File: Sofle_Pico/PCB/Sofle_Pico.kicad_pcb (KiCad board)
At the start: 2 copper layers, 145.4 x 116.3 mm, 124 parts, among them J1 Conn_01x05, J2 4PIN, J3 Conn_01x04, J4 Conn_01x04, J5 Conn_02x05_Odd_Even, J7 Conn_01x04, Q1 Si2301CDS, SW1 SW_PUSH, SW10 SW_PUSH, SW11 SW_PUSH, SW12 SW_PUSH, SW13 SW_PUSH, SW14 SW_PUSH, SW15 SW_PUSH, SW16 SW_PUSH, SW17 SW_PUSH, SW18 SW_PUSH, SW19 SW_PUSH, SW2 SW_PUSH, SW20 SW_PUSH, SW21 SW_PUSH, SW22 SW_PUSH, SW23 SW_PUSH, SW24 SW_PUSH, SW25 Rotary_Encoder_Switch-Device, SW26 SW_PUSH, SW27 SW_PUSH, SW28 SW_PUSH, SW29 SW_PUSH, SW3 SW_PUSH, SW30 SW_PUSH, SW4 SW_PUSH, SW5 SW_PUSH, SW6 SW_PUSH, SW7 SW_PUSH, SW8 SW_PUSH, SW9 SW_PUSH, U2 Pico

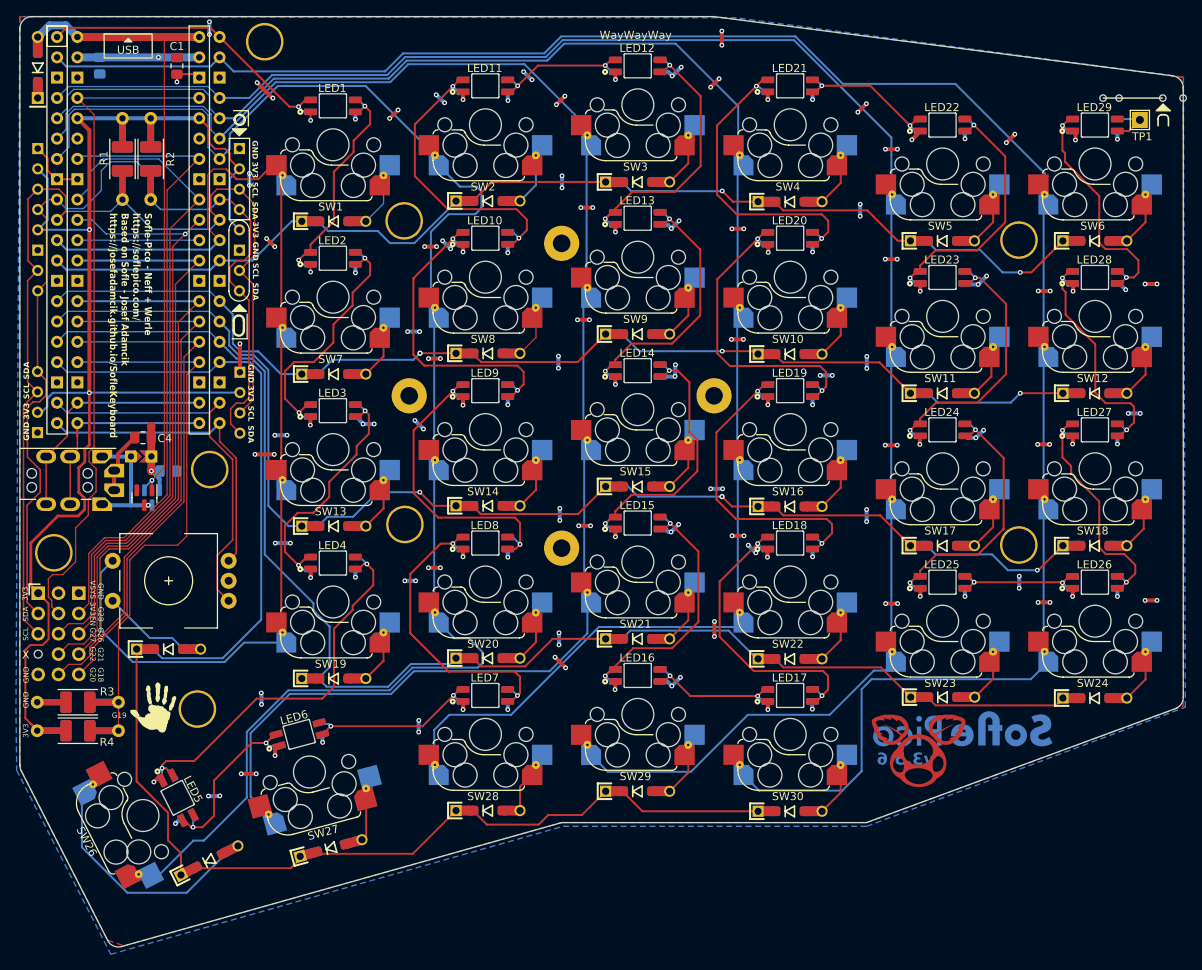
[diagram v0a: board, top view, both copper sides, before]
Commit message: Add a missing trace on F.Cu for the TSSR transistor VSYS terminal
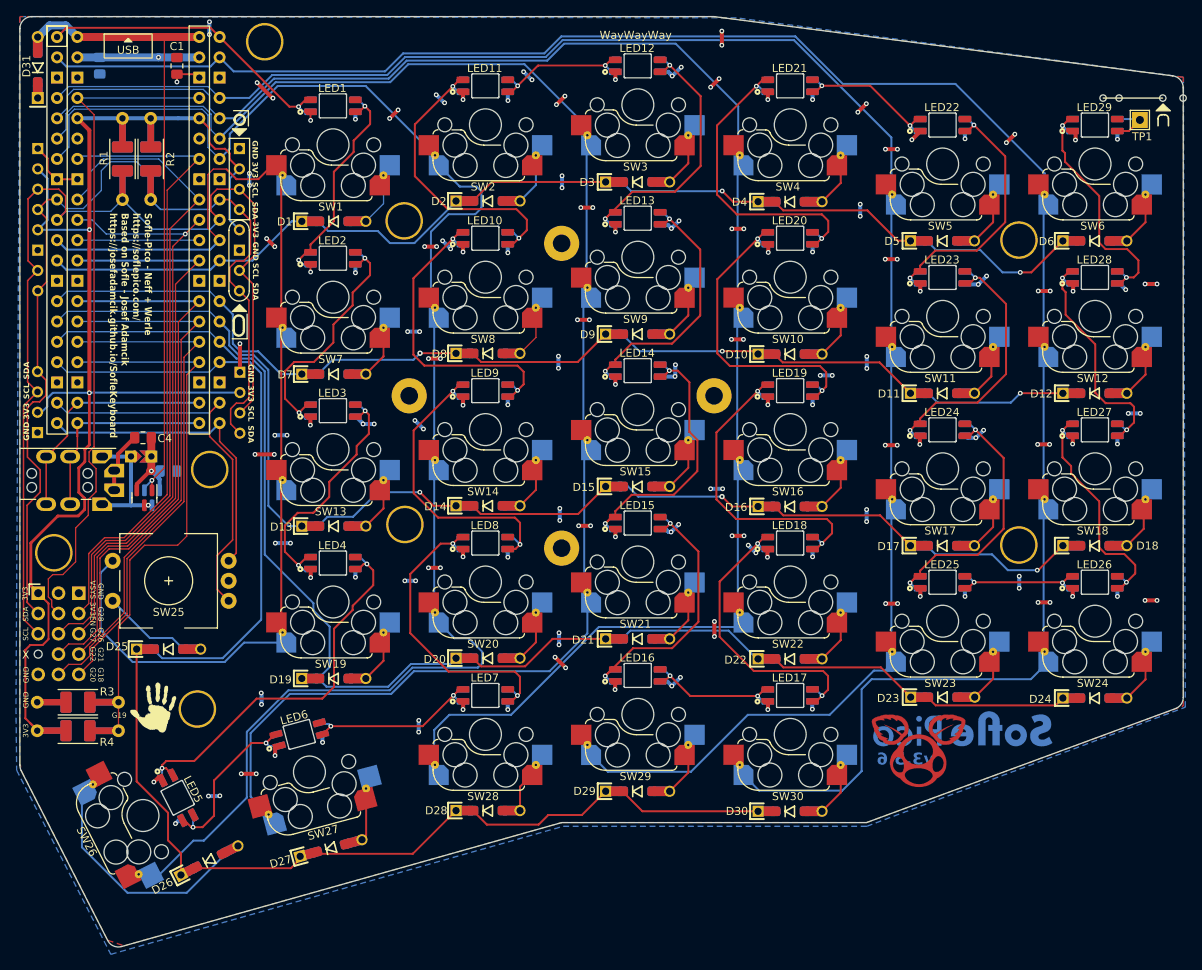
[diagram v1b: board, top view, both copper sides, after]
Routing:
- net VSYS: track 111.2 -> 113.0 mm
